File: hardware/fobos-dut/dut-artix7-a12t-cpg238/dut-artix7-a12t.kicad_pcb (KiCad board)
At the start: 4 copper layers, 88.9 x 76.2 mm, 203 parts, among them J1 Target, J10 Barrel_Jack_Switch, J2 Pmod 2x6, J3 575-8, J4 Glitch, J5 Conn_01x02, J6 Measure, J7 0878321420, J8 575-8, J9 Measure, Q1 FDS9435A, Q2 MMBT3904, Q3 BSS138, Q4 BSS138, Q5 BSS138, Q6 BSS138, Q7 BSS138, Q8 MMBT3904, SW1 SW_DIP_x03, SW2 SW_DIP_x03, U1 XC7A12T-CPG238, U10 SP3003-04ATG, U11 SP3003-04ATG, U2 SP3003-04ATG, U3 SP3003-04ATG, U4 SP3003-04ATG, U5 INA225, U6 BGA2801, U7 TS3A5018DBQR, U8 LTC3569EFE#PBF, U9 IS25LP256D-JMLE

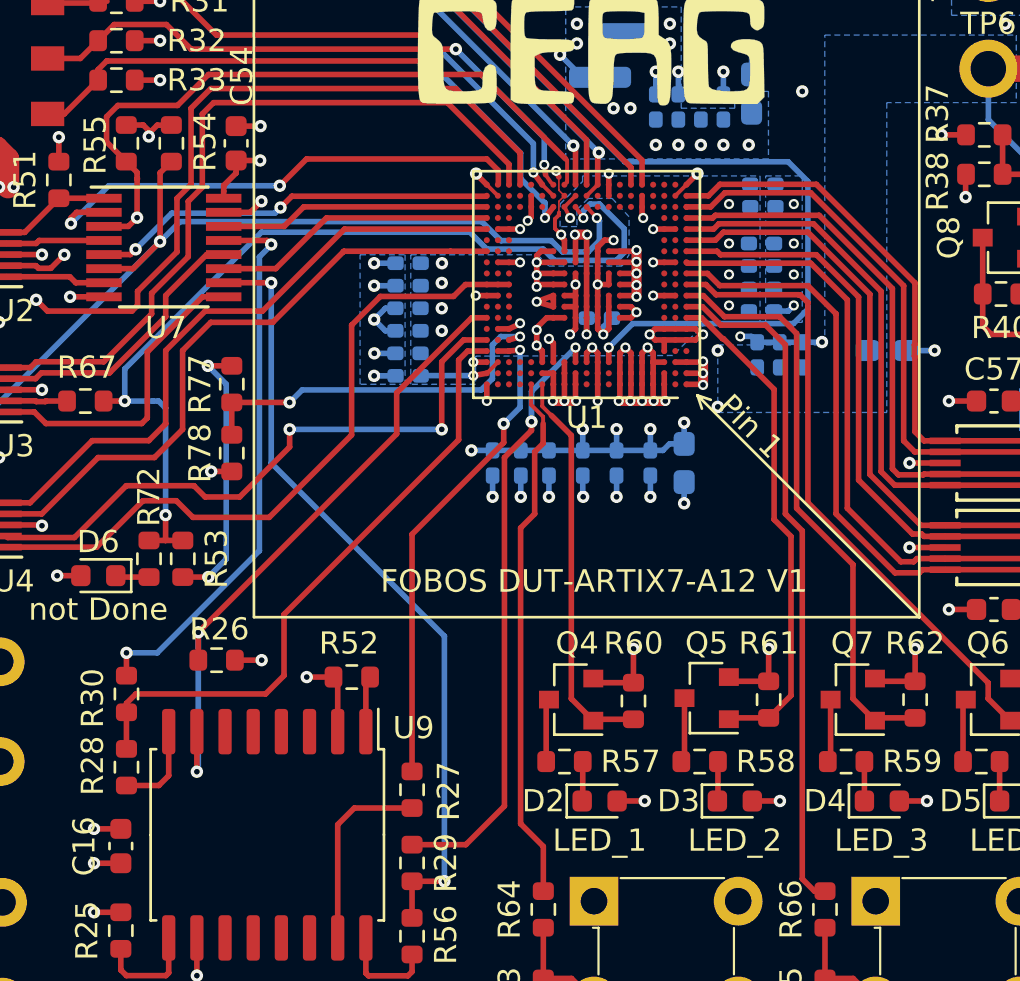
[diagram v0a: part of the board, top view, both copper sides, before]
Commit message: added copper corsers around FPGA
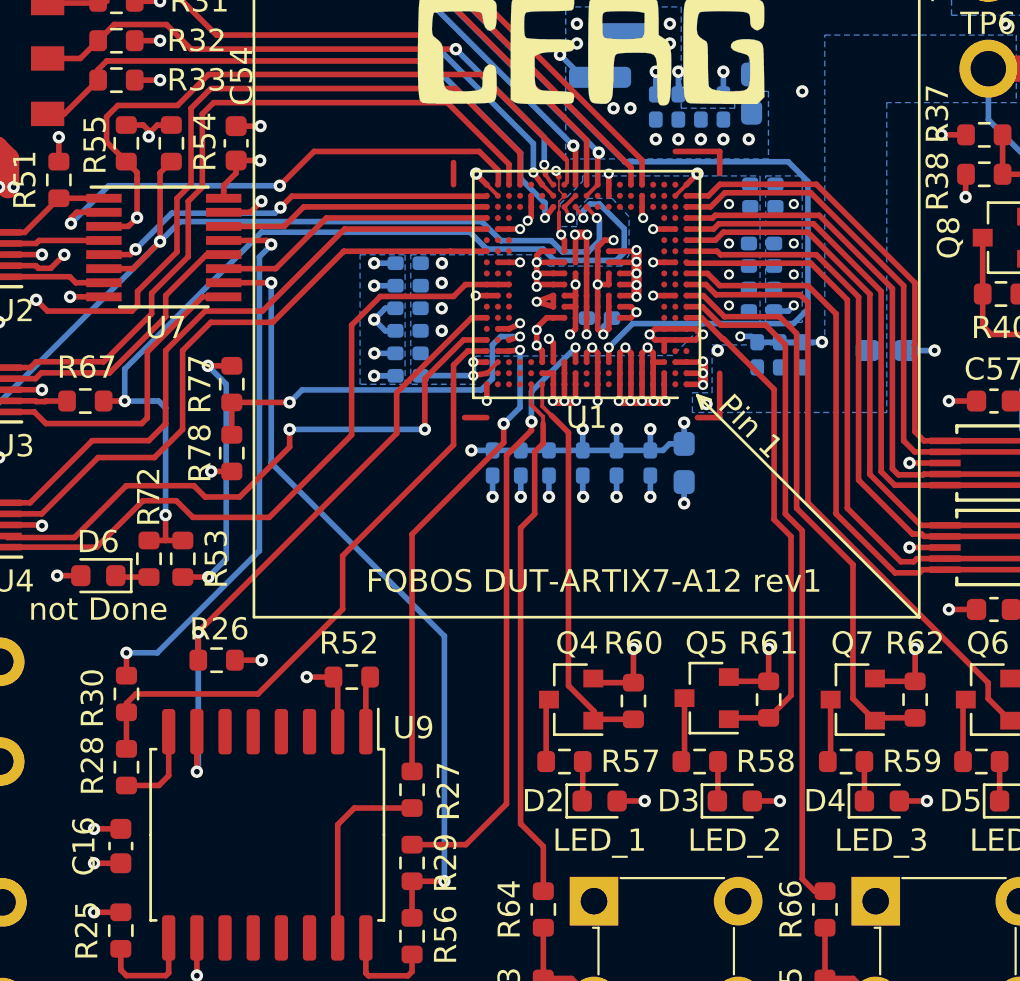
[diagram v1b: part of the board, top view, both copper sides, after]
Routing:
- net (no net): track 0.00 -> 8.00 mm
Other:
- net class Default: trace_width 0.0762 -> 0.127; via_dia 0.5588 -> 0.4572
- rule trace_min: 0.0762 -> 0.127
- board text added: "FOBOS DUT-ARTIX7-A12 rev1"
- board text removed: "FOBOS DUT-ARTIX7-A12 V1"

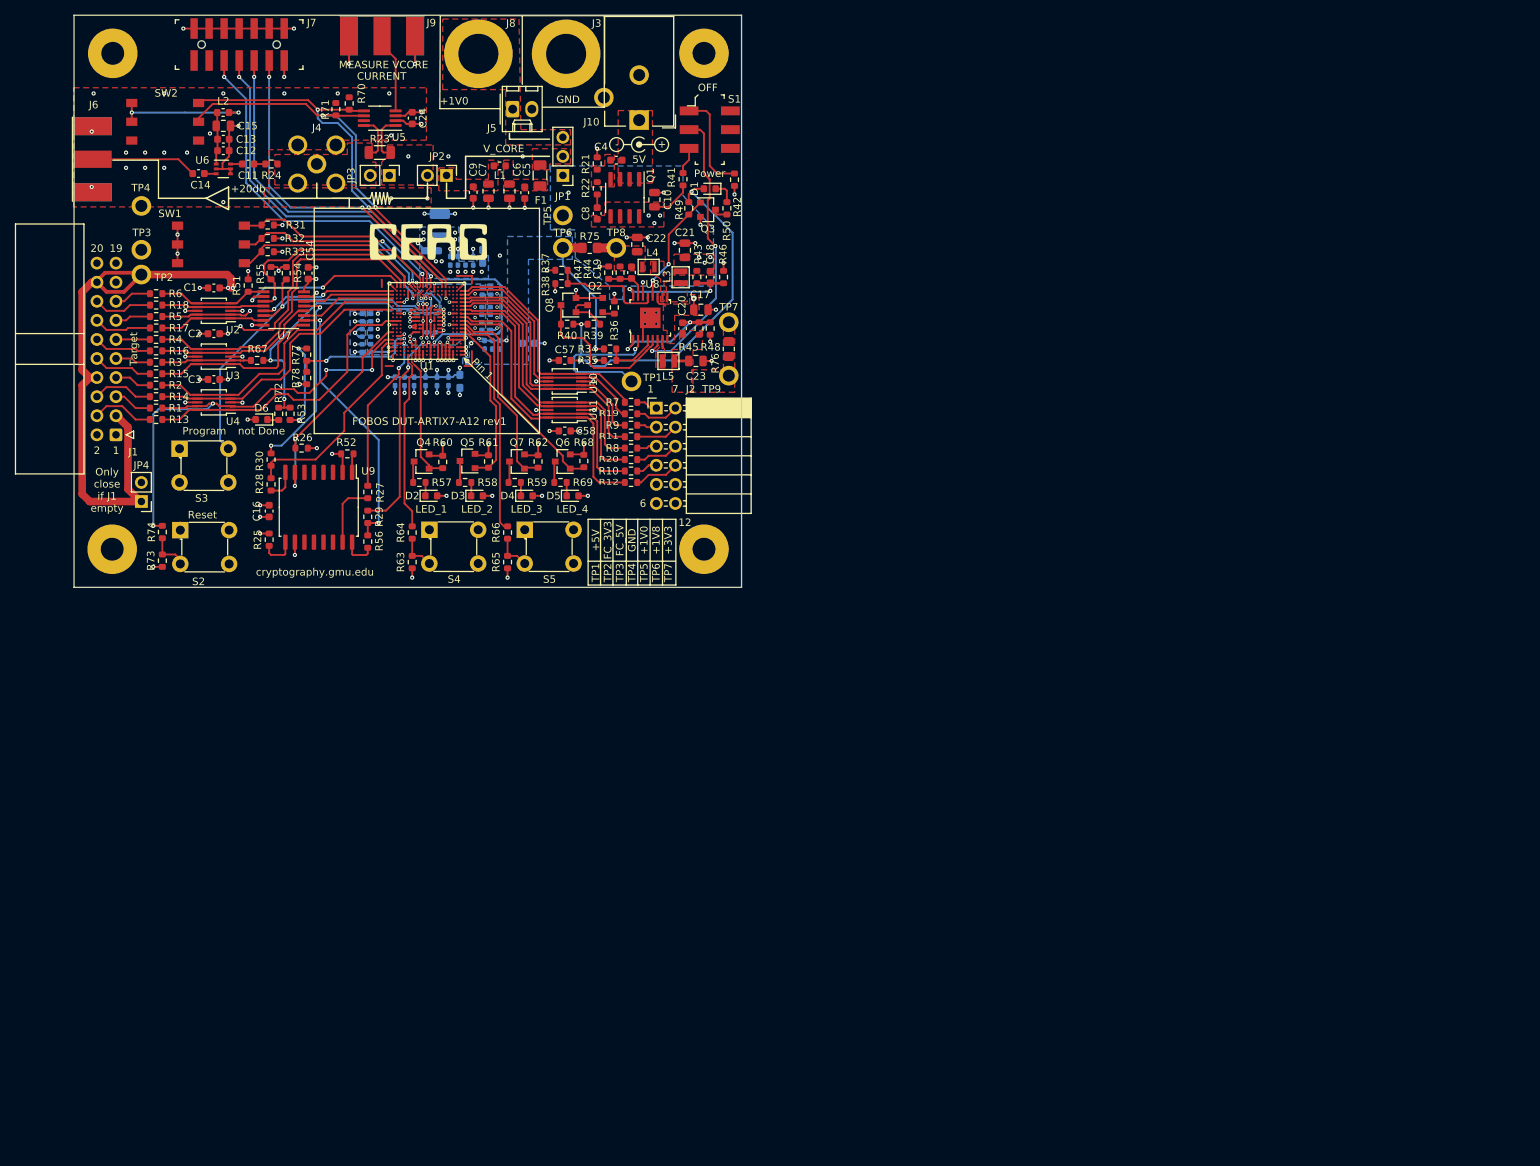
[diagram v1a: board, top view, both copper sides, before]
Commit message: Moved PCB so that it fits inside of title block Created BOM which matches the rev 1 design Generated pick and place data, assembly drawings
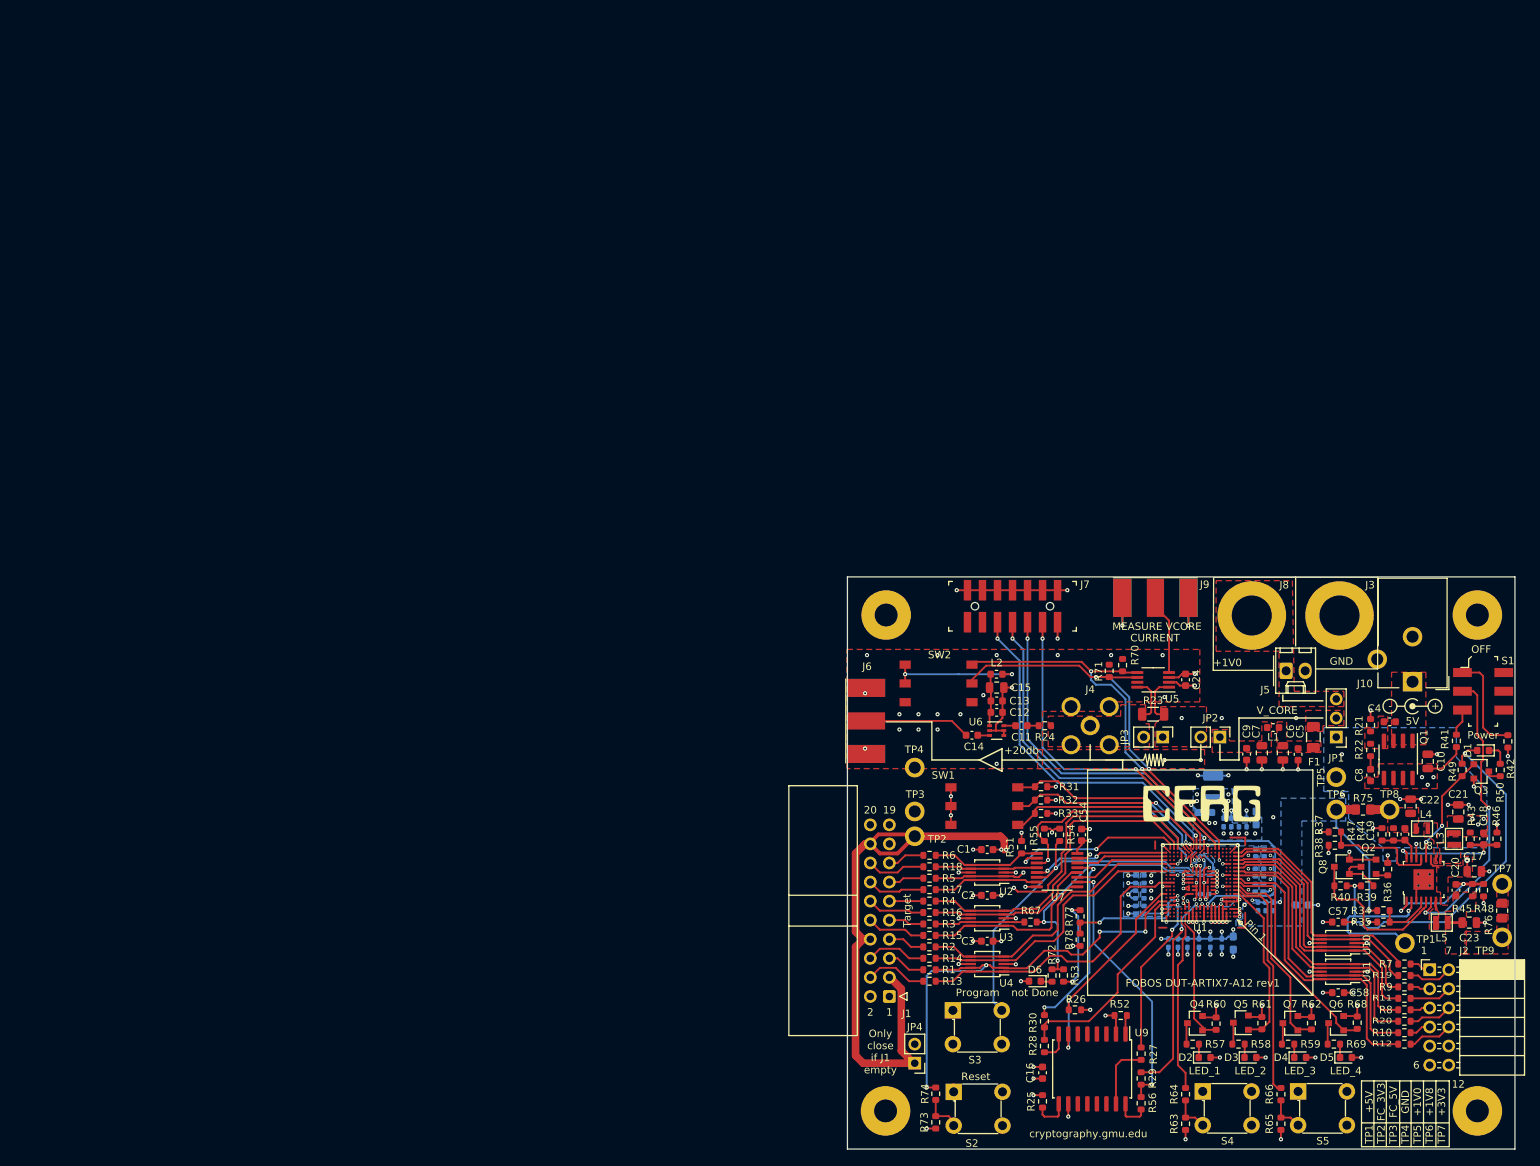
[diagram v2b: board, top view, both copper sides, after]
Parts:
- moved C1 127.3 mm to (121.6, 107.5)
- moved C12 127.3 mm to (122.9, 89.2)
- moved C13 127.3 mm to (122.9, 87.7)
- moved C15 127.3 mm to (122.9, 85.9)
- moved C2 127.3 mm to (121.6, 113.6)
- moved C25 127.3 mm to (141.9, 116.0)
- moved C28 127.3 mm to (148.3, 119.9)
- moved C3 127.3 mm to (121.6, 119.7)
- moved C30 127.3 mm to (152.9, 119.9)
- moved C31 127.3 mm to (149.8, 119.9)
- moved C33 127.3 mm to (141.9, 112.0)
- moved C35 127.3 mm to (141.9, 110.9)
- moved C36 127.3 mm to (151.3, 119.9)
- moved C37 127.3 mm to (154.4, 119.9)
- moved C39 127.3 mm to (163.5, 114.9)
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
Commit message: added BOM to artix-7 target board
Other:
- net class Default removed

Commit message: transitioned artix-7 dut to Kikad 6
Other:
- board text added: "VCCINT"
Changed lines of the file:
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@@
     (tags "capacitor handsolder")
     (attr smd)
-    (fp_text reference "C42" (at -0.008 2.4765) (layer "B.SilkS")
+    (fp_text reference "C42" (at 1.782 2.4765) (layer "B.SilkS")
       (effects (font (size 1 1) (thickness 0.15)) (justify mirror))
     )
@@
   (gr_line (start 164.98366 126.90088) (end 164.98366 96.90088) (layer "B.SilkS") (width 0.12))
   (gr_line (start 144.87366 117.01088) (end 144.87366 106.79088) (layer "B.SilkS") (width 0.12))
+  (gr_rect (start 145.35666 96.84288) (end 159.96166 105.73288) (layer "B.SilkS") (width 0.12) (fill none))
   (gr_line (start 164.98366 126.90088) (end 134.98366 126.90088) (layer "B.SilkS") (width 0.12))
   (gr_line (start 155.10366 106.79088) (end 155.13566 117.02088) (layer "B.SilkS") (width 0.12))
@@
   (gr_line (start 191.897 71.18088) (end 102.997 71.18088) (layer "Edge.Cuts") (width 0.05))
   (gr_line (start 102.997 147.38088) (end 191.897 147.38088) (layer "Edge.Cuts") (width 0.05))
+  (gr_text "VCCINT" (at 148.53166 104.46288) (layer "B.SilkS")
+    (effects (font (size 1 1) (thickness 0.15)) (justify mirror))
+  )
+  (gr_text "VCCINT" (at 147.89666 115.89288) (layer "B.SilkS")
+    (effects (font (size 1 1) (thickness 0.15)) (justify mirror))
+  )
   (gr_text "+5V\nFC_3V3\nFC_5V\nGND\n+1V0\n+1V8\n+3V3" (at 177.30566 141.10288 90) (layer "F.SilkS")
     (effects (font (size 1 1) (thickness 0.15)))
